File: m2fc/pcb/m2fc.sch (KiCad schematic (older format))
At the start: 53 parts, among them IC101 ADP3335, IC102 STM32F405VGT, P101 CONN_2, P102 CONN_2, P103 SWD, U101 BAT BOX, U102 ARM SW, U103 HOUSING, U104 HOUSING, U105 MICROSD, X101 8M

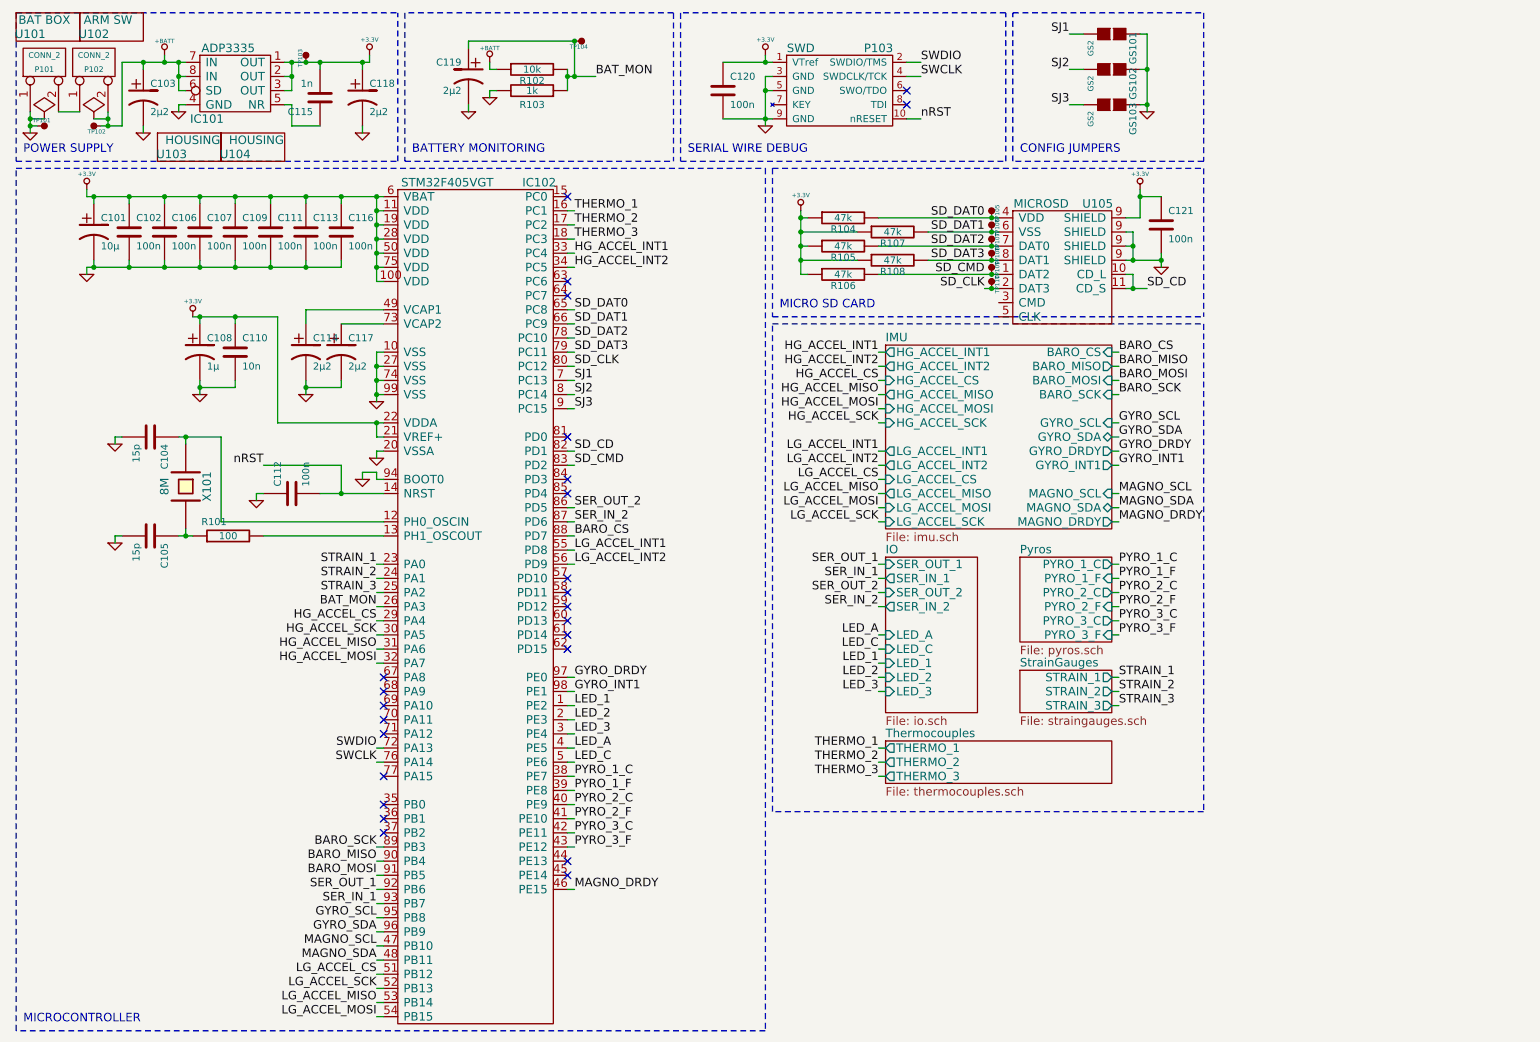
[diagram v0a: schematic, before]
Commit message: add esd diodes to m2fc
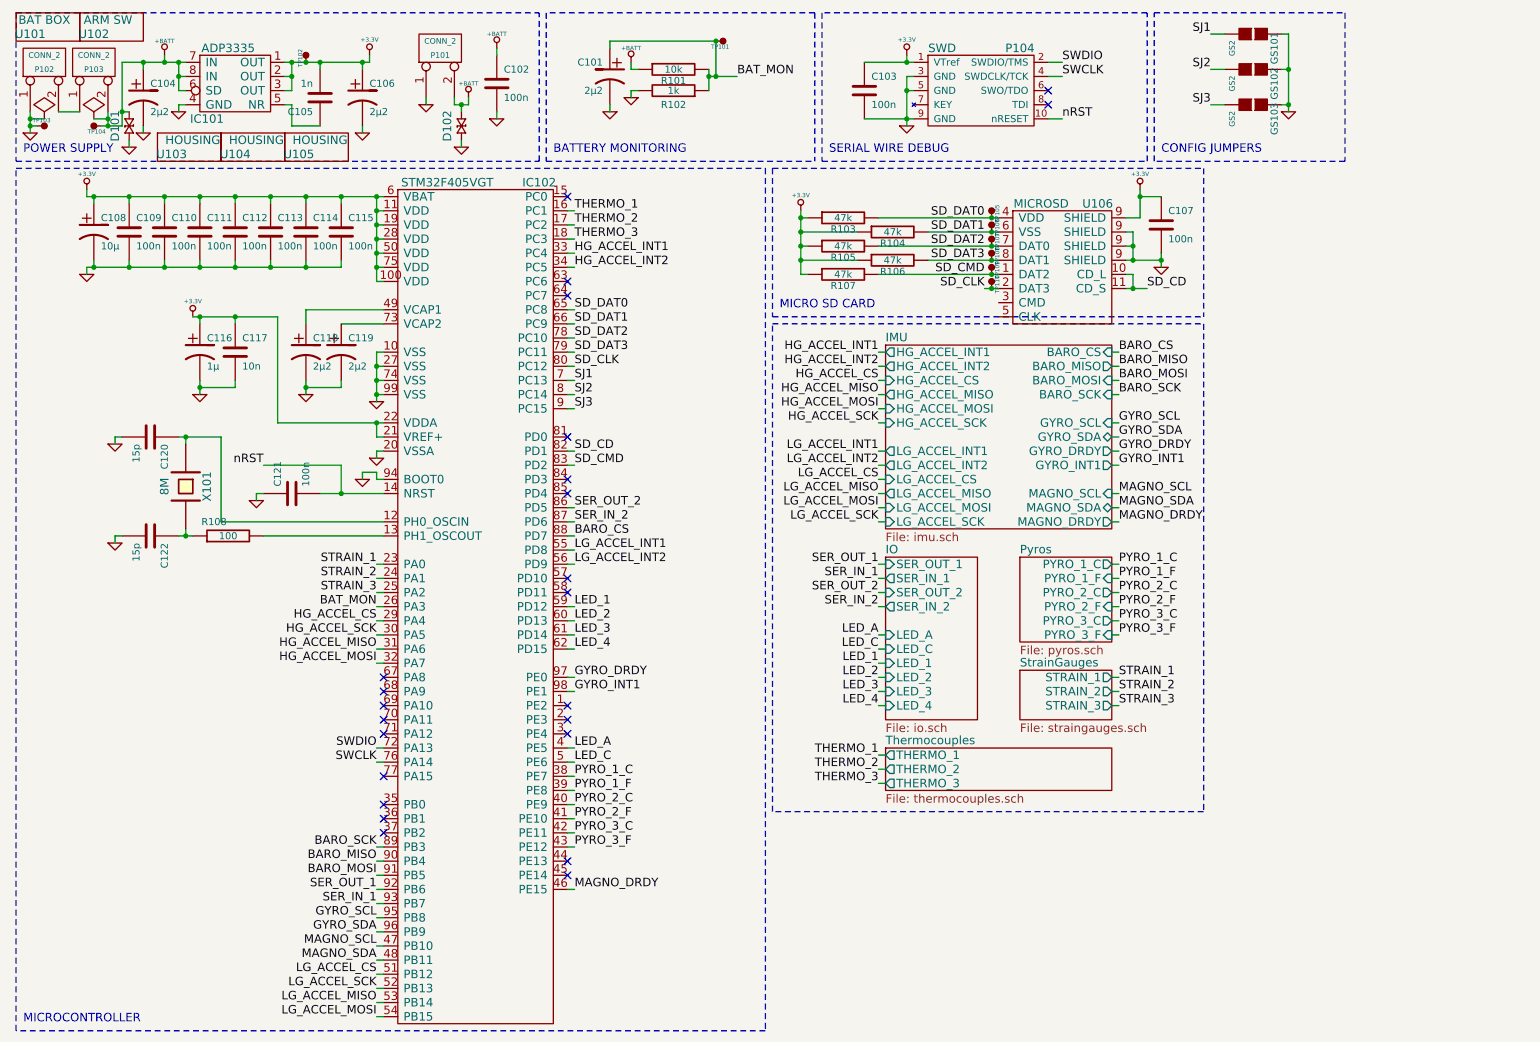
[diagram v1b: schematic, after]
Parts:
- added C102: 100n, m2fc:C0603, symbol C
- added D101, D102: CGA0402MLC-12G, m2fc:R0402, symbol CGA0402MLC-12G
- added P101: CONN_2, m2fc:S02B-PASK-2, symbol CONN_2
- added U105: HOUSING, symbol PART
- C108: renamed from C101; footprint 1411 -> m2fc:C0603; Farnell 2333026 -> 1657936
- C116: renamed from C108; footprint 0805 -> m2fc:C0603; Farnell 1658211 -> 2346895
- renumbered C119 to C101, C120 to C103, C103 to C104, C115 to C105, C118 to C106, C121 to C107, C102 to C109, C106 to C110, C107 to C111, C109 to C112, C111 to C113, C113 to C114, C116 to C115, C110 to C117, C114 to C118, C117 to C119, C104 to C120, C112 to C121, C105 to C122, P101 to P102, P102 to P103, P103 to P104, R102 to R101, R103 to R102, R104 to R103, R107 to R104, R108 to R106, R106 to R107, R101 to R108, TP104 to TP101, TP103 to TP102, TP101 to TP103, TP102 to TP104, U105 to U106
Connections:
- net +BATT: now also C102.1, D101.1, D102.1, P101.2 (PM)
- net GND: now also C102.2, D101.2, D102.2, P101.1 (P1)
- net LED_1: now also IC102.59 (PD12); no longer IC102.1 (PE2)
- net LED_2: now also IC102.60 (PD13); no longer IC102.2 (PE3)
- net LED_3: now also IC102.61 (PD14); no longer IC102.3 (PE4)
- net LED_4: now reaches IC102.62 (PD15)
- no-connect marks 25 -> 24
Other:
- moved on the sheet: C101, C103, GS101, GS102, GS103, P104, R101, R102, TP101

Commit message: m2fc footprints, start layout
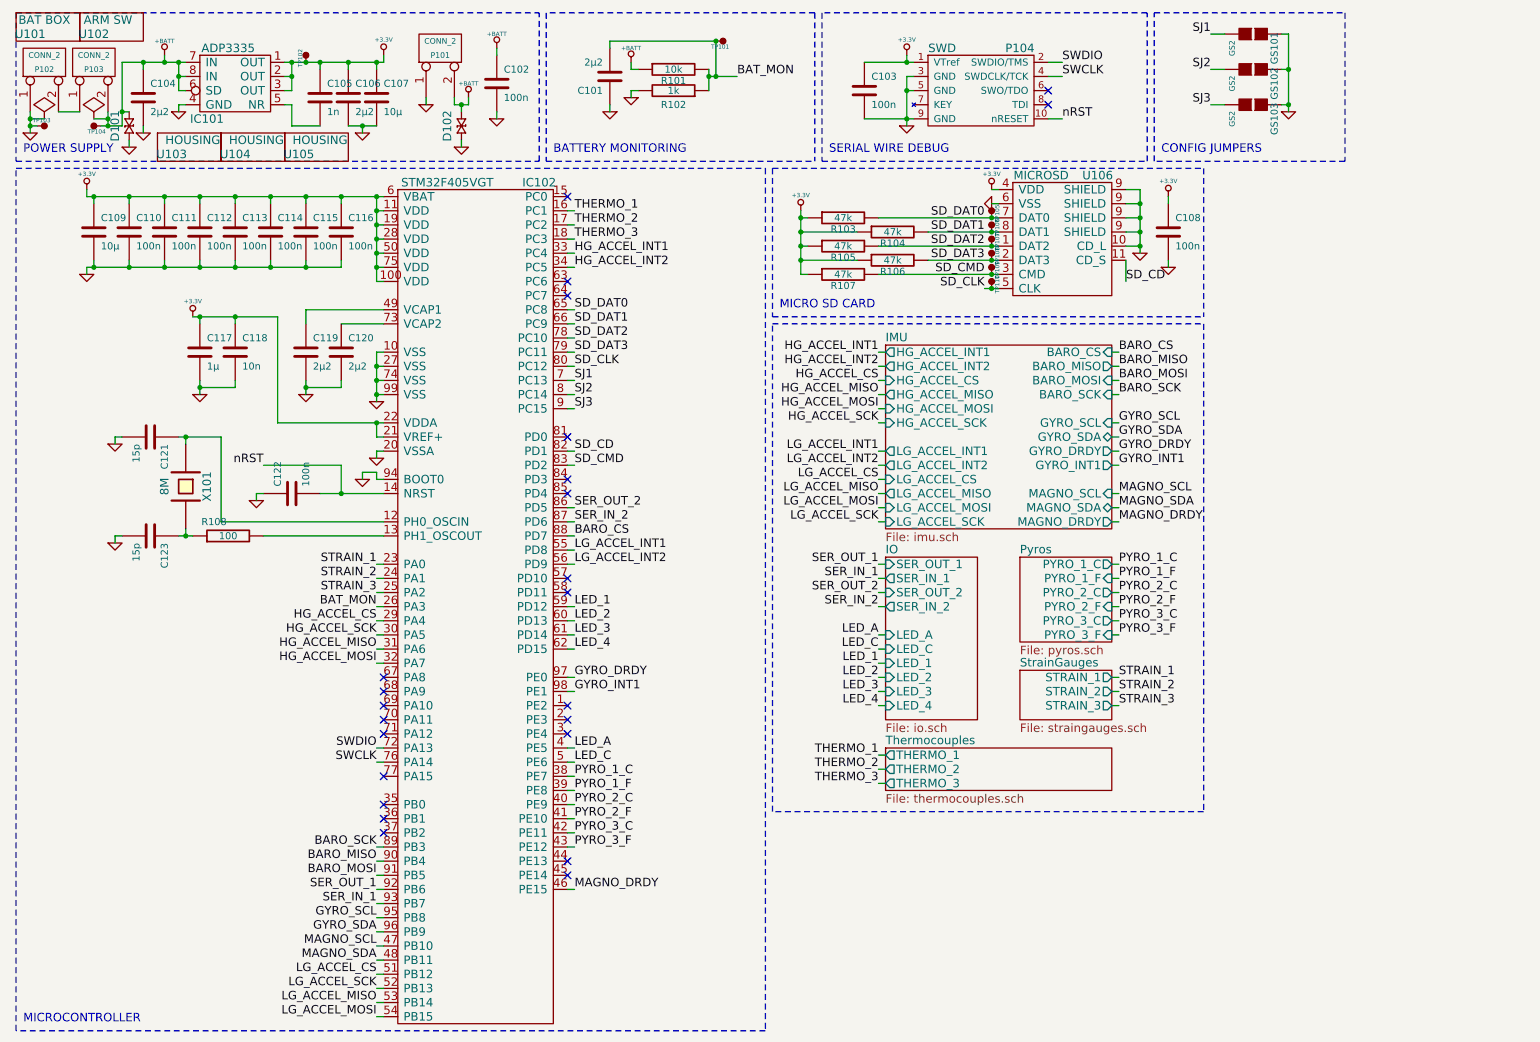
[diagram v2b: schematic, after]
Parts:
- removed C101, C104, C106, C118, C119: 2µ2, m2fc:C0603, symbol CP1
- removed C108: 10µ, m2fc:C0603, symbol CP1
- removed C116: 1µ, m2fc:C0603, symbol CP1
- added C101, C104, C106, C119, C120: 2µ2, m2fc:C0603, symbol C
- added C107, C109: 10µ, m2fc:C0603, symbol C
- added C117: 1µ, m2fc:C0603, symbol C
- IC102: footprint (none) -> m2fc:LQFP100
- U102: Farnell 149288 -> SW04244
- U106: footprint (none) -> m2fc:MICROSD; Farnell 2081363 -> 2334075
- renumbered C107 to C108, C109 to C110, C110 to C111, C111 to C112, C112 to C113, C113 to C114, C114 to C115, C115 to C116, C117 to C118, C120 to C121, C121 to C122, C122 to C123
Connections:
- net +3.3V: now also C105.1, U106.4 (VDD), C106.1, C107.1, C109.1, C117.1; no longer C105.2, U106.9 (SHIELD)
- net +BATT: now also C104.1
- net BAT_MON: now also C101.2
- net GND: now also U106.10 (CD_L), U106.6 (VSS), C101.1, C104.2, C106.2, C107.2, C109.2, C117.2, C119.2, C120.2
- net SD_CD: no longer U106.10 (CD_L)
- net SD_CLK: now also U106.5 (CLK); no longer U106.2 (DAT3)
- net SD_CMD: now also U106.3 (CMD); no longer U106.1 (DAT2)
- net SD_DAT0: now also U106.7 (DAT0); no longer U106.4 (VDD)
- net SD_DAT1: now also U106.8 (DAT1); no longer U106.6 (VSS)
- net SD_DAT2: now also U106.1 (DAT2); no longer U106.7 (DAT0)
- net SD_DAT3: now also U106.2 (DAT3); no longer U106.8 (DAT1)
- net at IC102.49 (VCAP1): now also C119.1
- net at IC102.73 (VCAP2): now also C120.1
- net at IC101.5 (NR): now also C105.2; no longer C105.1
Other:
- moved on the sheet: C108, U106

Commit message: layout going ok so far...
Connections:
- net GYRO_DRDY: now also IC102.45 (PE14); no longer IC102.97 (PE0)
- net GYRO_INT1: now also IC102.46 (PE15); no longer IC102.98 (PE1)
- net GYRO_SCL: now also IC102.47 (PB10); no longer IC102.95 (PB8)
- net GYRO_SDA: now also IC102.48 (PB11); no longer IC102.96 (PB9)
- net MAGNO_DRDY: now also IC102.97 (PE0); no longer IC102.46 (PE15)
- net MAGNO_SCL: now also IC102.95 (PB8); no longer IC102.47 (PB10)
- net MAGNO_SDA: now also IC102.96 (PB9); no longer IC102.48 (PB11)
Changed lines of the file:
@@
 Text Label 3050 6800 2    60   ~ 0
 SER_IN_1
+Text Label 3050 7100 2    60   ~ 0
+GYRO_SCL
+Text Label 3050 7200 2    60   ~ 0
+GYRO_SDA
 Text Label 3050 6900 2    60   ~ 0
-GYRO_SCL
+MAGNO_SCL
 Text Label 3050 7000 2    60   ~ 0
-GYRO_SDA
-Text Label 3050 7100 2    60   ~ 0
-MAGNO_SCL
-Text Label 3050 7200 2    60   ~ 0
 MAGNO_SDA
 Text Label 3050 7300 2    60   ~ 0
@@
 Text Label 4450 4400 0    60   ~ 0
 LG_ACCEL_INT2
-Text Label 4450 5200 0    60   ~ 0
+Text Label 4450 6600 0    60   ~ 0
 GYRO_DRDY
 Text Label 4450 4200 0    60   ~ 0
 BARO_CS
-Text Label 4450 6700 0    60   ~ 0
+Text Label 4450 5200 0    60   ~ 0
 MAGNO_DRDY
 Text Label 4450 5700 0    60   ~ 0
@@
 Text Label 8300 3700 0    60   ~ 0
 GYRO_INT1
-Text Label 4450 5300 0    60   ~ 0
+Text Label 4450 6700 0    60   ~ 0
 GYRO_INT1
 Text Label 6600 5950 2    60   ~ 0
@@
 NoConn ~ 4400 4600
 NoConn ~ 4400 6500
-NoConn ~ 4400 6600
 NoConn ~ 3100 6100
 NoConn ~ 3100 6200
@@
 	3050 6800 3100 6800
 Wire Wire Line
+	3050 7100 3100 7100
+Wire Wire Line
+	3050 7200 3100 7200
+Wire Wire Line
 	3050 6900 3100 6900
 Wire Wire Line
 	3050 7000 3100 7000
 Wire Wire Line
-	3050 7100 3100 7100
-Wire Wire Line
-	3050 7200 3100 7200
-Wire Wire Line
 	3050 7300 3100 7300
 Wire Wire Line
@@
 	3050 7600 3100 7600
 Wire Wire Line
-	4450 6700 4400 6700
-Wire Wire Line
 	4450 6200 4400 6200
 Wire Wire Line
@@
 	4400 4700 4450 4700
 Wire Wire Line
-	4400 5300 4450 5300
-Wire Wire Line
-	4400 5200 4450 5200
+	4400 6700 4450 6700
+Wire Wire Line
+	4400 6600 4450 6600
 Wire Wire Line
 	4400 4400 4450 4400
@@
 Wire Wire Line
 	8350 2250 8350 2400
+Wire Wire Line
+	4400 5200 4450 5200
+NoConn ~ 4400 5300
 $EndSCHEMATC

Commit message: paid off woo
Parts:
- added C124, C126: 2µ2, m2fc:C0603, symbol C
- added C125: 1n, m2fc:C0603, symbol C
- added IC103: ADP3335, m2fc:MSOP8, symbol ADP3335
- added TP111: TESTPAD, m2fc:TESTPAD, symbol TESTPAD
- added U107, U108, U109, U110, U111, U112: MOUNT, m2fc:M3_MOUNT, symbol PART
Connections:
- net +3.3V: no longer C117.1, C118.1, IC102.21 (VREF+), IC102.22 (VDDA)
- net +BATT: now also P103.1 (P1), C124.1, IC103.6 (SD), IC103.7 (IN), IC103.8 (IN); no longer P103.2 (PM)
- net GND: now also P102.2 (PM), C124.2, C126.2, IC103.4 (GND); no longer P102.1 (P1)
- net SJ1: now also IC102.69 (PA10); no longer IC102.7 (PC13)
- net SJ2: now also IC102.70 (PA11); no longer IC102.8 (PC14)
- net SJ3: now also IC102.71 (PA12); no longer IC102.9 (PC15)
- new net: P102.1 (P1), P103.2 (PM)
- new net: C125.2, IC103.5 (NR)
- new net VAA: C117.1, C118.1, C125.1, C126.1, IC102.21 (VREF+), IC102.22 (VDDA), IC103.1 (OUT), IC103.2 (OUT), IC103.3 (OUT), TP111.1 (TP)
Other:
- moved on the sheet: C101, C102, C103, D102, GS101, GS102, GS103, P101, P104, R101, R102, TP101

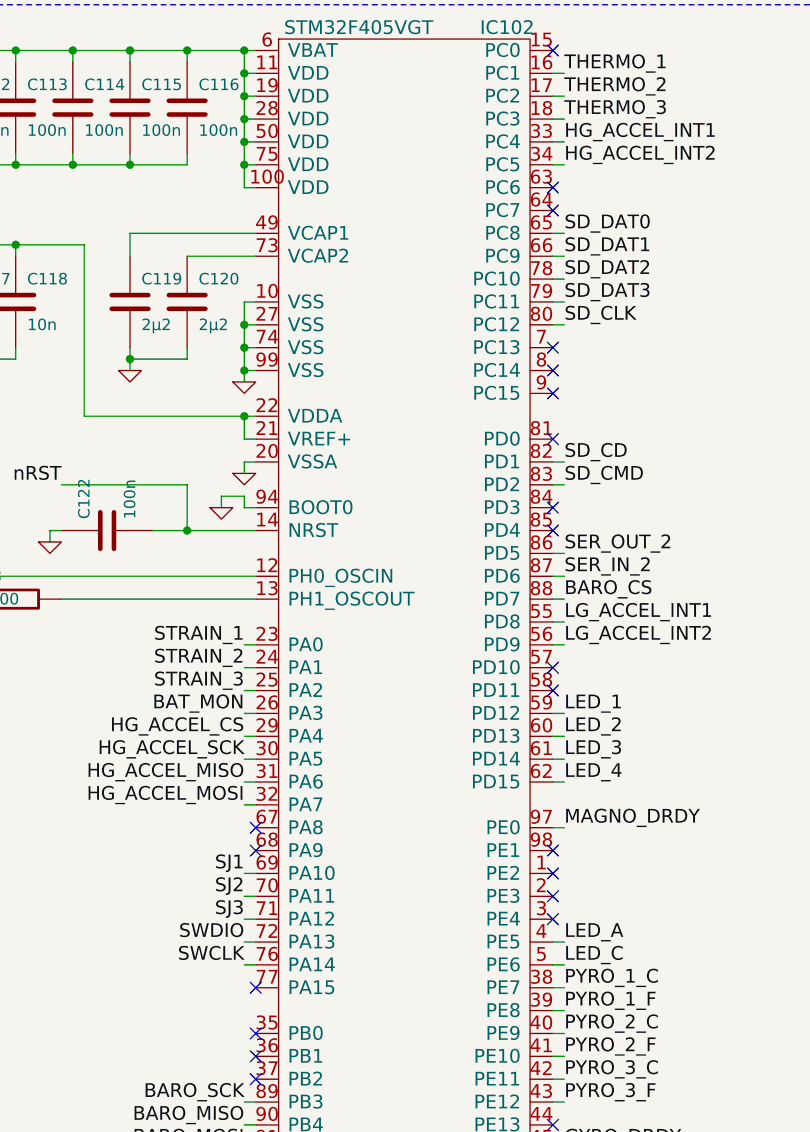
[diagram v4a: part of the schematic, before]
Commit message: swap crystal to smt. ready 2 route!!
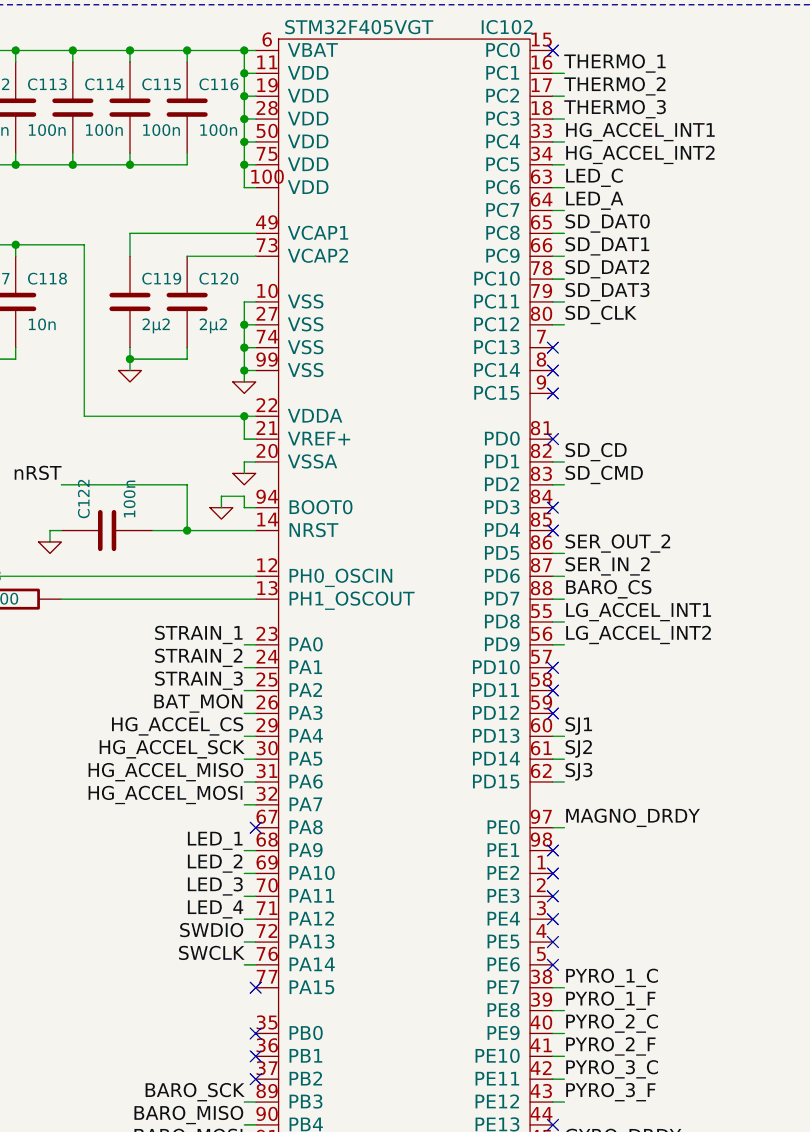
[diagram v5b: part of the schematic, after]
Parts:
- X101: footprint m2fc:HC49S -> m2fc:XTAL50x32; Farnell 2063945 -> 2101329
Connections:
- net LED_1: now also IC102.68 (PA9); no longer IC102.59 (PD12)
- net LED_2: now also IC102.69 (PA10); no longer IC102.60 (PD13)
- net LED_3: now also IC102.70 (PA11); no longer IC102.61 (PD14)
- net LED_4: now also IC102.71 (PA12); no longer IC102.62 (PD15)
- net LED_A: now also IC102.64 (PC7); no longer IC102.4 (PE5)
- net LED_C: now also IC102.63 (PC6); no longer IC102.5 (PE6)
- net SJ1: now also IC102.60 (PD13); no longer IC102.69 (PA10)
- net SJ2: now also IC102.61 (PD14); no longer IC102.70 (PA11)
- net SJ3: now also IC102.62 (PD15); no longer IC102.71 (PA12)
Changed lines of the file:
@@
 F 0 "X101" H 1700 4000 60  0000 C CNN
 F 1 "8M" H 1700 3700 60  0000 C CNN
-F 2 "m2fc:HC49S" H 1700 3850 60  0001 C CNN
+F 2 "m2fc:XTAL50x32" H 1700 3850 60  0001 C CNN
 F 3 "" H 1700 3850 60  0001 C CNN
-F 4 "2063945" H 1700 3850 60  0001 C CNN "Farnell"
+F 4 "2101329" H 1700 3850 60  0001 C CNN "Farnell"
 	1    1700 3850
 	0    1    1    0
@@
 Text Label 4450 5200 0    60   ~ 0
 MAGNO_DRDY
-Text Label 4450 5700 0    60   ~ 0
+Text Label 4450 2500 0    60   ~ 0
 LED_A
-Text Label 4450 5800 0    60   ~ 0
+Text Label 4450 2400 0    60   ~ 0
 LED_C
-Text Label 4450 4700 0    60   ~ 0
+Text Label 3050 5300 2    60   ~ 0
 LED_1
-Text Label 4450 4800 0    60   ~ 0
+Text Label 3050 5400 2    60   ~ 0
 LED_2
-Text Label 4450 4900 0    60   ~ 0
+Text Label 3050 5500 2    60   ~ 0
 LED_3
 Text Label 4450 5900 0    60   ~ 0
@@
 THERMO_3
 NoConn ~ 4400 1800
-NoConn ~ 4400 2400
-NoConn ~ 4400 2500
 NoConn ~ 4400 3500
 NoConn ~ 4400 3800
@@
 NoConn ~ 3100 6300
 NoConn ~ 3100 5900
-NoConn ~ 3100 5300
 NoConn ~ 3100 5200
 Text Label 8300 4900 0    60   ~ 0
@@
 Text Label 10250 1150 2    60   ~ 0
 SJ3
-Text Label 3050 5400 2    60   ~ 0
+Text Label 4450 4800 0    60   ~ 0
 SJ1
-Text Label 3050 5500 2    60   ~ 0
+Text Label 4450 4900 0    60   ~ 0
 SJ2
-Text Label 3050 5600 2    60   ~ 0
+Text Label 4450 5000 0    60   ~ 0
 SJ3
 $Comp
@@
 Text Label 6600 5400 2    60   ~ 0
 LED_4
-Text Label 4450 5000 0    60   ~ 0
+Text Label 3050 5600 2    60   ~ 0
 LED_4
 NoConn ~ 4400 5400
@@
 	4400 5900 4450 5900
 Wire Wire Line
-	4400 5800 4450 5800
-Wire Wire Line
-	4400 5700 4450 5700
-Wire Wire Line
-	4400 4800 4450 4800
-Wire Wire Line
-	4400 4700 4450 4700
+	4400 2500 4450 2500
+Wire Wire Line
+	4400 2400 4450 2400
+Wire Wire Line
+	3100 5400 3050 5400
+Wire Wire Line
+	3100 5300 3050 5300
 Wire Wire Line
 	4400 6700 4450 6700
@@
 	9850 1550 9850 500
 Wire Wire Line
-	3100 5400 3050 5400
-Wire Wire Line
-	3100 5500 3050 5500
-Wire Wire Line
-	3100 5600 3050 5600
+	4400 4800 4450 4800
+Wire Wire Line
+	4400 4900 4450 4900
+Wire Wire Line
+	4400 5000 4450 5000
 Wire Wire Line
 	6050 1900 6050 2350
@@
 	6600 5400 6650 5400
 Wire Wire Line
-	4400 4900 4450 4900
-Wire Wire Line
-	4400 5000 4450 5000
+	3100 5500 3050 5500
+Wire Wire Line
+	3100 5600 3050 5600
 Wire Wire Line
 	5050 1150 5050 1200
@@
 NoConn ~ 4400 3200
 NoConn ~ 4400 3300
+NoConn ~ 4400 4700
+NoConn ~ 4400 5700
+NoConn ~ 4400 5800
 $EndSCHEMATC
